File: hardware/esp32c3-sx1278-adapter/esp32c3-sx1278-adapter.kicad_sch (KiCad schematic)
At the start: 4 parts, among them J1 Conn_01x08, J2 Conn_01x08, J3 Antenna, U2 SX1278_module

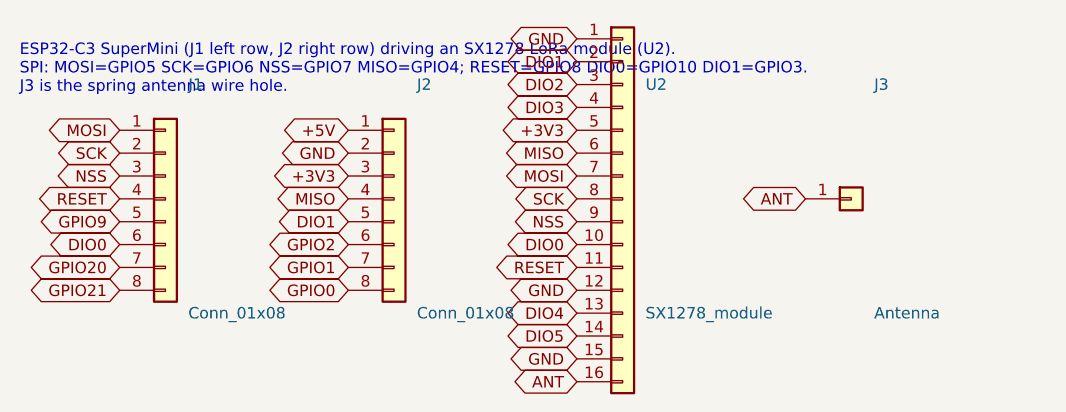
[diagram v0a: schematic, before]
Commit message: CC1101 adapter GND pour with antenna keepout; optional SMA on the SX1278 adapter
* kicadgen: Zone (copper pour / keepout) support, board revision "0" in
  every title block, KICAD_SHARE overridable for non-snap installs.
* scripts/fill_zones.py: fills zones with KiCad's own filler (pcbnew python,
  re-executed inside the snap when needed) and splices only the fill
  polygons into the generated file, so generation stays reproducible.
* CC1101 adapter: GND pour on F.Cu (all tracks remain on B.Cu), keepout on
  both layers under the SuperMini's ceramic antenna; MISO/GDO2 now run
  outside the SuperMini body instead of under its antenna.
* SX1278 adapter: 24 x 58 mm, optional edge-mount SMA jack (J4) on the
  bottom edge fed from the wire-hole antenna trace, ground legs on B.Cu
  with vias to the front pads.

Co-Authored-By: Claude Fable 5.1 <noreply@anthropic.com>
Claude-Session: https://claude.ai/code/session_01JoGdh4Cg3VtTTDZi4gQuiN
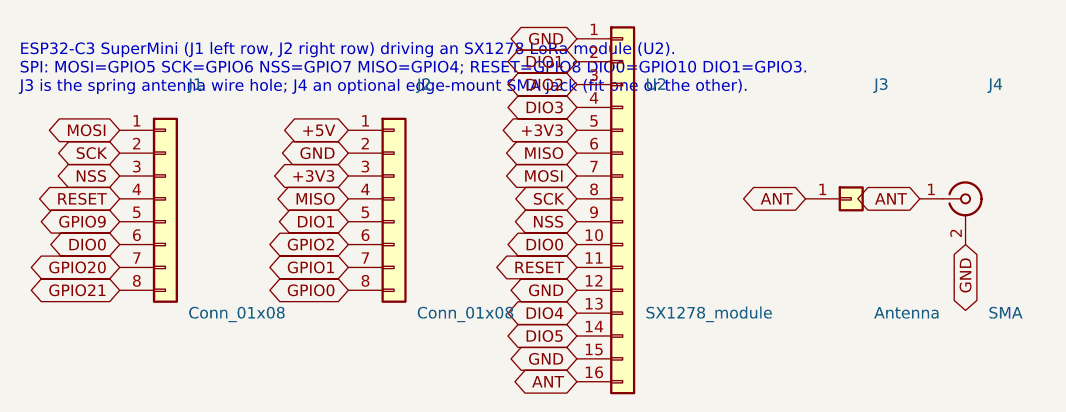
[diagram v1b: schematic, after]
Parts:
- added J4: SMA, Adapter:SMA_EdgeMount_E07, symbol Connector:Conn_Coaxial
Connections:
- net ANT: now also J4.1 (In)
- net GND: now also J4.2 (Ext)
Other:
- note added: "ESP32-C3 SuperMini (J1 left row, J2 right row) driving an SX1278 LoRa module (U2). SPI: MOSI=GPIO5 SCK=GPIO6 NSS=GPIO7 MISO=GPIO4; RESET=GPIO8 DIO0=GPIO10 DIO1=GPIO3. J3 is the spring antenna wire hole; J4 an optional edge-mount SMA jack (fit one or the other)."
- note removed: "ESP32-C3 SuperMini (J1 left row, J2 right row) driving an SX1278 LoRa module (U2). SPI: MOSI=GPIO5 SCK=GPIO6 NSS=GPIO7 MISO=GPIO4; RESET=GPIO8 DIO0=GPIO10 DIO1=GPIO3. J3 is the spring antenna wire hole."
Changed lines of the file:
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@@
 	(title_block
 		(title "ESP32-C3 SuperMini to SX1278 LoRa module adapter")
-		(rev "1")
+		(rev "0")
 		(comment 1 "Carrier joining an ESP32-C3 SuperMini to a 16-pin castellated SX1278 433MHz module")
 	)
@@
 		)
 	)
-	(text "ESP32-C3 SuperMini (J1 left row, J2 right row) driving an SX1278 LoRa module (U2).\nSPI: MOSI=GPIO5 SCK=GPIO6 NSS=GPIO7 MISO=GPIO4; RESET=GPIO8 DIO0=GPIO10 DIO1=GPIO3.\nJ3 is the spring antenna wire hole."
+	(symbol
+		(lib_id "Connector:Conn_Coaxial")
+		(at 165.1 101.6 0)
+		(unit 1)
+		(exclude_from_sim no)
+		(in_bom yes)
+		(on_board yes)
+		(dnp no)
+		(fields_autoplaced yes)
+		(property "Reference" "J4"
+			(at 167.64 88.9 0)
+			(effects
+				(font
+					(size 1.27 1.27)
+				)
+				(justify left)
+			)
+		)
+		(property "Value" "SMA"
+			(at 167.64 114.3 0)
+			(effects
+				(font
+					(size 1.27 1.27)
+				)
+				(justify left)
+			)
+		)
+		(property "Footprint" "Adapter:SMA_EdgeMount_E07"
+			(at 165.1 101.6 0)
+			(effects
+				(font
+					(size 1.27 1.27)
+				)
+				(hide yes)
+			)
+		)
+		(property "Datasheet" "~"
+			(at 165.1 101.6 0)
+			(effects
+				(font
+					(size 1.27 1.27)
+				)
+				(hide yes)
+			)
+		)
+		(property "Description" "Optional edge-mount SMA jack"
+			(at 165.1 101.6 0)
+			(effects
+				(font
+					(size 1.27 1.27)
+				)
+				(hide yes)
+			)
+		)
+		(pin "1"
+		)
+		(pin "2"
+		)
+		(instances
+			(project "esp32c3-sx1278-adapter"
+				(path "/b71943b6-a88f-5429-bfd6-fb1a52f93b27"
+					(reference "J4")
+					(unit 1)
+				)
+			)
+		)
+	)
+	(global_label "ANT"
+		(shape bidirectional)
+		(at 160.02 101.6 180)
+		(fields_autoplaced yes)
+		(effects
+			(font
+				(size 1.27 1.27)
+			)
+			(justify right)
+		)
+		(property "Intersheetrefs" "${INTERSHEET_REFS}"
+			(at 160.02 101.6 0)
+			(effects
+				(font
+					(size 1.27 1.27)
+				)
+				(justify right)
+				(hide yes)
+			)
+		)
+	)
+	(global_label "GND"
+		(shape bidirectional)
+		(at 165.1 106.68 270)
+		(fields_autoplaced yes)
+		(effects
+			(font
+				(size 1.27 1.27)
+			)
+			(justify right)
+		)
+		(property "Intersheetrefs" "${INTERSHEET_REFS}"
+			(at 165.1 106.68 0)
+			(effects
+				(font
+					(size 1.27 1.27)
+				)
+				(justify right)
+				(hide yes)
+			)
+		)
+	)
+	(text "ESP32-C3 SuperMini (J1 left row, J2 right row) driving an SX1278 LoRa module (U2).\nSPI: MOSI=GPIO5 SCK=GPIO6 NSS=GPIO7 MISO=GPIO4; RESET=GPIO8 DIO0=GPIO10 DIO1=GPIO3.\nJ3 is the spring antenna wire hole; J4 an optional edge-mount SMA jack (fit one or the other)."
 		(exclude_from_sim no)
 		(at 60 90 0)
